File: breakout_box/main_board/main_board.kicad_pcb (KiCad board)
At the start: 2 copper layers, 56 x 120 mm, 45 parts, among them CN1 19PIN_LEMO, Q1 DMP3099L, Q2 MJD122, Q3 MMBT5401, Q4 DMP3099L

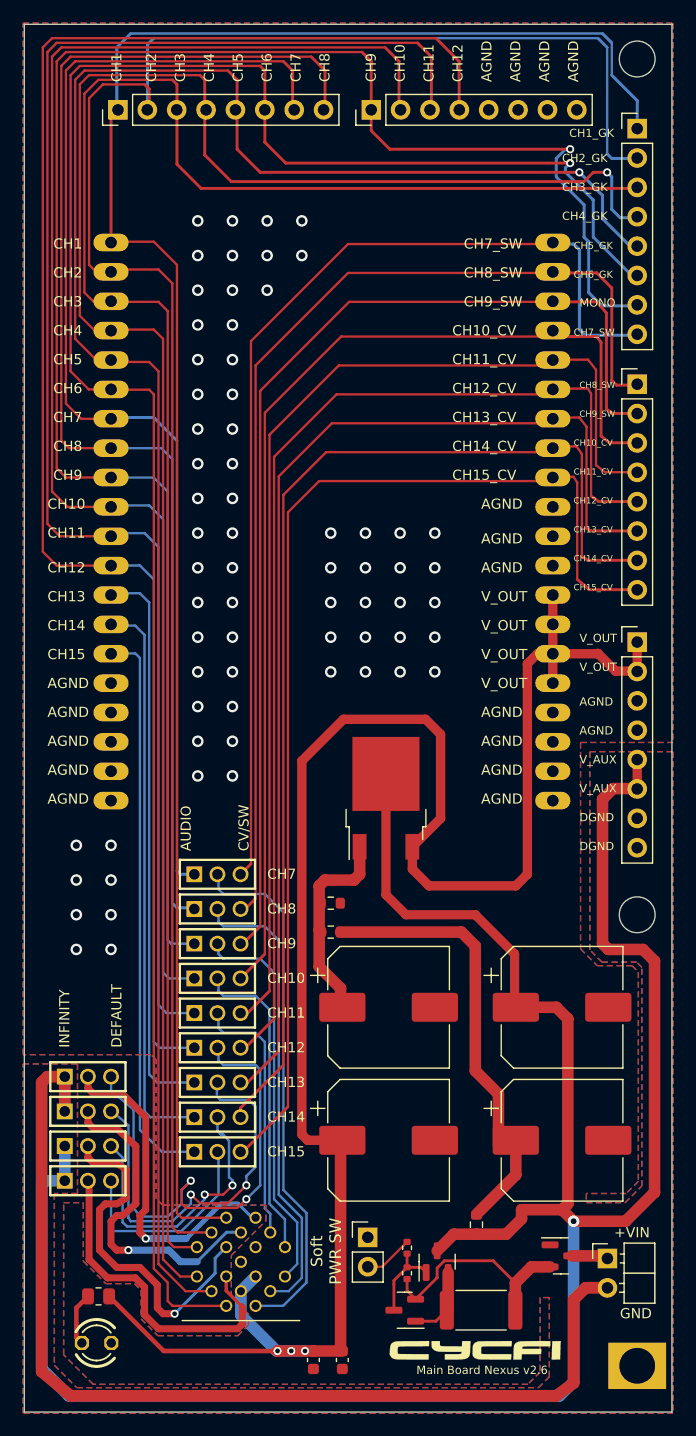
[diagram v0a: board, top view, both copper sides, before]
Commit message: Change the component to C2977785, plus various PCB refinements
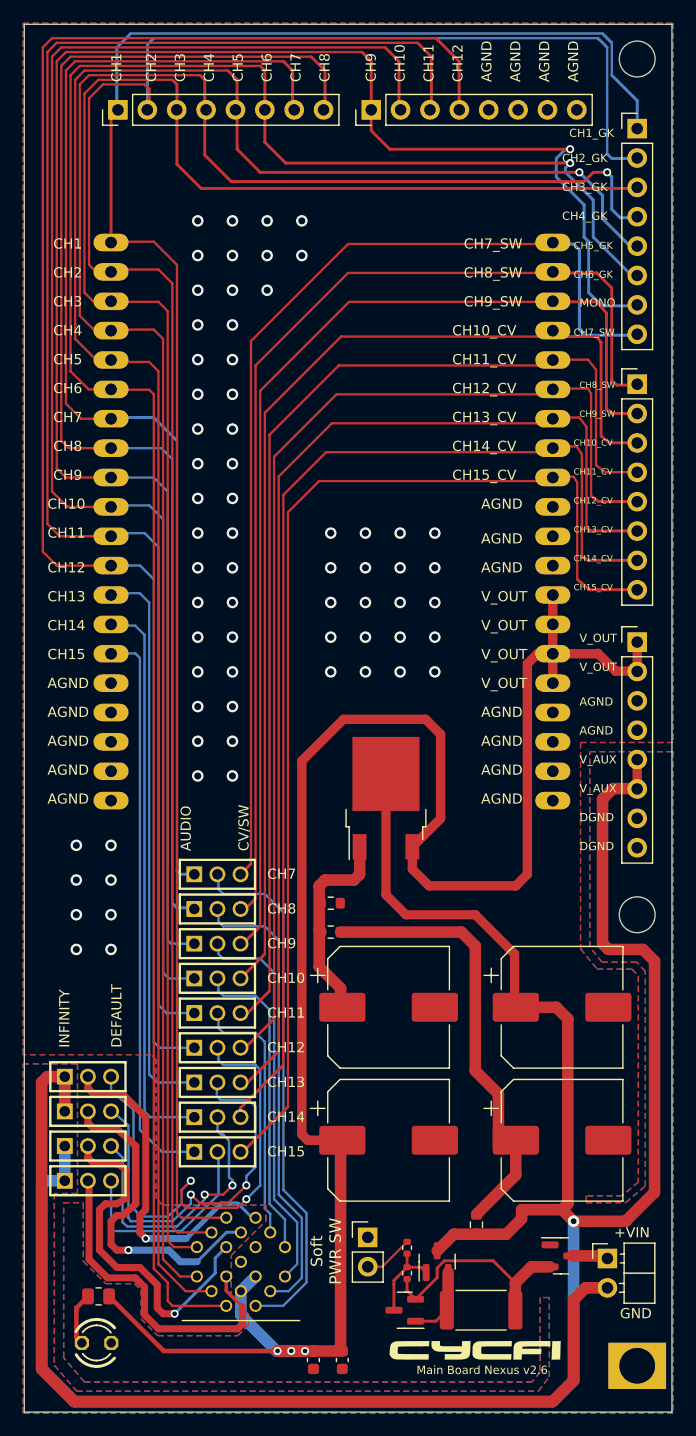
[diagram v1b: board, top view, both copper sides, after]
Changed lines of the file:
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@@
     (effects (font (size 0.536448 0.536448) (thickness 0.073152)) (justify left bottom))
   )
-  (segment (start 168.0011 162.5036) (end 168.0011 155.2989) (width 1.016) (layer "F.Cu") (net 1))
   (segment (start 124.0011 136.0036) (end 124.0011 139.0036) (width 1.016) (layer "F.Cu") (net 1))
+  (segment (start 124.0011 136.0036) (end 122.5011 136.0036) (width 1.016) (layer "F.Cu") (net 1))
+  (segment (start 166.174316 164.1) (end 168.0011 162.273216) (width 1.016) (layer "F.Cu") (net 1))
+  (segment (start 122.0011 136.5036) (end 122.0011 161.3011) (width 1.016) (layer "F.Cu") (net 1))
+  (segment (start 122.5011 136.0036) (end 122.0011 136.5036) (width 1.016) (layer "F.Cu") (net 1))
+  (segment (start 122.0011 161.3011) (end 124.8 164.1) (width 1.016) (layer "F.Cu") (net 1))
   (segment (start 168.0011 155.2989) (end 169.035 154.265) (width 1.016) (layer "F.Cu") (net 1))
-  (segment (start 124.0011 136.0036) (end 122.5011 136.0036) (width 1.016) (layer "F.Cu") (net 1))
+  (segment (start 124.8 164.1) (end 166.174316 164.1) (width 1.016) (layer "F.Cu") (net 1))
   (segment (start 169.035 154.265) (end 170.925 154.265) (width 1.016) (layer "F.Cu") (net 1))
-  (segment (start 166.5011 163.6036) (end 168.0011 162.5036) (width 1.016) (layer "F.Cu") (net 1))
-  (segment (start 124.5011 163.6036) (end 166.5011 163.6036) (width 1.016) (layer "F.Cu") (net 1))
-  (segment (start 122.5011 136.0036) (end 122.0011 136.5036) (width 1.016) (layer "F.Cu") (net 1))
-  (segment (start 122.0011 161.5036) (end 124.5011 163.6036) (width 1.016) (layer "F.Cu") (net 1))
-  (segment (start 122.0011 136.5036) (end 122.0011 161.5036) (width 1.016) (layer "F.Cu") (net 1))
+  (segment (start 168.0011 162.273216) (end 168.0011 155.2989) (width 1.016) (layer "F.Cu") (net 1))
   (via (at 128 119) (size 1) (drill 0.6) (layers "F.Cu" "B.Cu") (free) (net 1))
   (via (at 135.5 95) (size 1) (drill 0.6) (layers "F.Cu" "B.Cu") (free) (net 1))
@@
   (segment (start 170.5011 124.5036) (end 171.0011 125.0036) (width 1) (layer "F.Cu") (net 18))
   (via (at 168.0011 148.5036) (size 1) (drill 0.5) (layers "F.Cu" "B.Cu") (net 18))
-  (segment (start 124.3511 163.6036) (end 166.7964 163.6036) (width 1) (layer "B.Cu") (net 18))
-  (segment (start 122.2511 145.0036) (end 124.0011 145.0036) (width 1) (layer "B.Cu") (net 18))
-  (segment (start 124.3511 163.6036) (end 122.0011 161.2536) (width 1) (layer "B.Cu") (net 18))
-  (segment (start 168.0011 162.3989) (end 168.0011 148.5036) (width 1) (layer "B.Cu") (net 18))
-  (segment (start 166.7964 163.6036) (end 168.0011 162.3989) (width 1) (layer "B.Cu") (net 18))
+  (segment (start 124.0011 145.0036) (end 122.2511 145.0036) (width 1) (layer "B.Cu") (net 18))
+  (segment (start 122.2511 145.0036) (end 122.0011 145.2536) (width 1) (layer "B.Cu") (net 18))
+  (segment (start 122.0011 161.2536) (end 124.8475 164.1) (width 1) (layer "B.Cu") (net 18))
+  (segment (start 122.0011 145.2536) (end 122.0011 161.2536) (width 1) (layer "B.Cu") (net 18))
+  (segment (start 166.2 164.1) (end 168.0011 162.2989) (width 1) (layer "B.Cu") (net 18))
   (segment (start 124.0011 142.0036) (end 124.0011 145.0036) (width 1) (layer "B.Cu") (net 18))
-  (segment (start 122.0011 161.2536) (end 122.0011 145.2536) (width 1) (layer "B.Cu") (net 18))
-  (segment (start 122.0011 145.2536) (end 122.2511 145.0036) (width 1) (layer "B.Cu") (net 18))
+  (segment (start 124.8475 164.1) (end 166.2 164.1) (width 1) (layer "B.Cu") (net 18))
+  (segment (start 168.0011 162.2989) (end 168.0011 148.5036) (width 1) (layer "B.Cu") (net 18))
   (segment (start 140.1011 117.6036) (end 139.2011 118.5036) (width 0.254) (layer "F.Cu") (net 19))
   (segment (start 148.4964 64.0036) (end 166.0711 64.0036) (width 0.2032) (layer "F.Cu") (net 19))
@@
   (segment (start 151.45 152.44) (end 153.6 150.29) (width 0.2) (layer "F.Cu") (net 48))
   (segment (start 150.2 152.44) (end 151.45 152.44) (width 0.2) (layer "F.Cu") (net 48))
-  (zone (net 1) (net_name "GND") (layer "F.Cu") (hatch edge 0.508)
+  (zone (net 1) (net_name "GND") (layers F&B.Cu) (hatch edge 0.508)
     (priority 6)
     (connect_pads (clearance 0.000001))
@@
         (xy 168.6027 107.1052)
         (xy 168.6027 124.961516)
-        (xy 170.043184 126.402)
-        (xy 173.043184 126.402)
-        (xy 173.6027 126.961516)
-        (xy 173.6027 145.045684)
-        (xy 172.543184 146.1052)
-        (xy 169.1027 146.1052)
+        (xy 170.043184 126.702)
+        (xy 173.043184 126.702)
+        (xy 173.6027 127.3)
+        (xy 173.6027 145.1)
+        (xy 172.2 146.3052)
+        (xy 169.1027 146.3052)
         (xy 169.1027 146.902)
-        (xy 172.459016 146.902)
-        (xy 173.8995 145.461516)
-        (xy 173.8995 126.545684)
+        (xy 172.5 146.9)
+        (xy 174.1995 145.461516)
+        (xy 174.2 126.9)
         (xy 173.459016 126.1052)
         (xy 170.459016 126.1052)
-        (xy 169.3995 125.045684)
+        (xy 169.4 124.8)
         (xy 169.3995 107.902)
         (xy 176.6027 107.902)
@@
         (xy 123.1027 146.1052)
         (xy 123.1027 160.961516)
-        (xy 125.043184 162.902)
-        (xy 164.959016 162.902)
+        (xy 125.043184 163.202)
+        (xy 164.959016 163.202)
         (xy 165.8995 161.961516)
         (xy 165.8995 155.1052)
         (xy 165.1027 155.1052)
         (xy 165.1027 161.545684)
-        (xy 164.043184 162.6052)
-        (xy 126.459016 162.6052)
-        (xy 123.8995 160.045684)
+        (xy 164.4 162.4052)
+        (xy 125.7 162.4052)
+        (xy 123.9 160.3)
         (xy 123.8995 146.902)
         (xy 125.6027 146.902)
-        (xy 125.6027 151.961516)
-        (xy 127.543184 153.902)
-        (xy 130.043184 153.902)
-        (xy 130.6027 154.461516)
-        (xy 130.6027 156.961516)
-        (xy 132.043184 158.402)
-        (xy 138.959016 158.402)
-        (xy 139.8995 157.461516)
-        (xy 139.8995 156.545684)
-        (xy 138.3995 155.045684)
-        (xy 138.3995 151.461516)
-        (xy 141.3995 148.461516)
-        (xy 141.3995 147.1052)
-        (xy 132.459016 147.1052)
-        (xy 131.8995 146.545684)
-        (xy 131.8995 134.545684)
-        (xy 131.459016 134.1052)
-        (xy 120.3995 134.1052)
-        (xy 120.3995 44.902)
-        (xy 176.6027 44.902)
-      )
-    )
-  )
-  (zone (net 1) (net_name "GND") (layer "B.Cu") (hatch edge 0.508)
-    (priority 6)
-    (connect_pads (clearance 0.000001))
-    (min_thickness 0.1016) (filled_areas_thickness no)
-    (fill yes (thermal_gap 0.2532) (thermal_bridge_width 0.2532))
-    (polygon
-      (pts
-        (xy 176.6027 107.1052)
-        (xy 168.6027 107.1052)
-        (xy 168.6027 124.961516)
-        (xy 170.043184 126.402)
-        (xy 173.043184 126.402)
-        (xy 173.6027 126.961516)
-        (xy 173.6027 145.045684)
-        (xy 172.543184 146.1052)
-        (xy 169.1027 146.1052)
-        (xy 169.1027 146.902)
-        (xy 172.459016 146.902)
-        (xy 173.8995 145.461516)
-        (xy 173.8995 126.545684)
-        (xy 173.459016 126.1052)
-        (xy 170.459016 126.1052)
-        (xy 169.3995 125.045684)
-        (xy 169.3995 107.902)
-        (xy 176.6027 107.902)
-        (xy 176.6027 165.1052)
-        (xy 120.3995 165.1052)
-        (xy 120.3995 134.902)
-        (xy 125.1027 134.902)
-        (xy 125.1027 146.1052)
-        (xy 123.1027 146.1052)
-        (xy 123.1027 160.961516)
-        (xy 125.043184 162.902)
-        (xy 164.959016 162.902)
-        (xy 165.8995 161.961516)
-        (xy 165.8995 155.1052)
-        (xy 165.1027 155.1052)
-        (xy 165.1027 161.545684)
-        (xy 164.043184 162.6052)
-        (xy 126.459016 162.6052)
-        (xy 123.8995 160.045684)
-        (xy 123.8995 146.902)
-        (xy 125.6027 146.902)

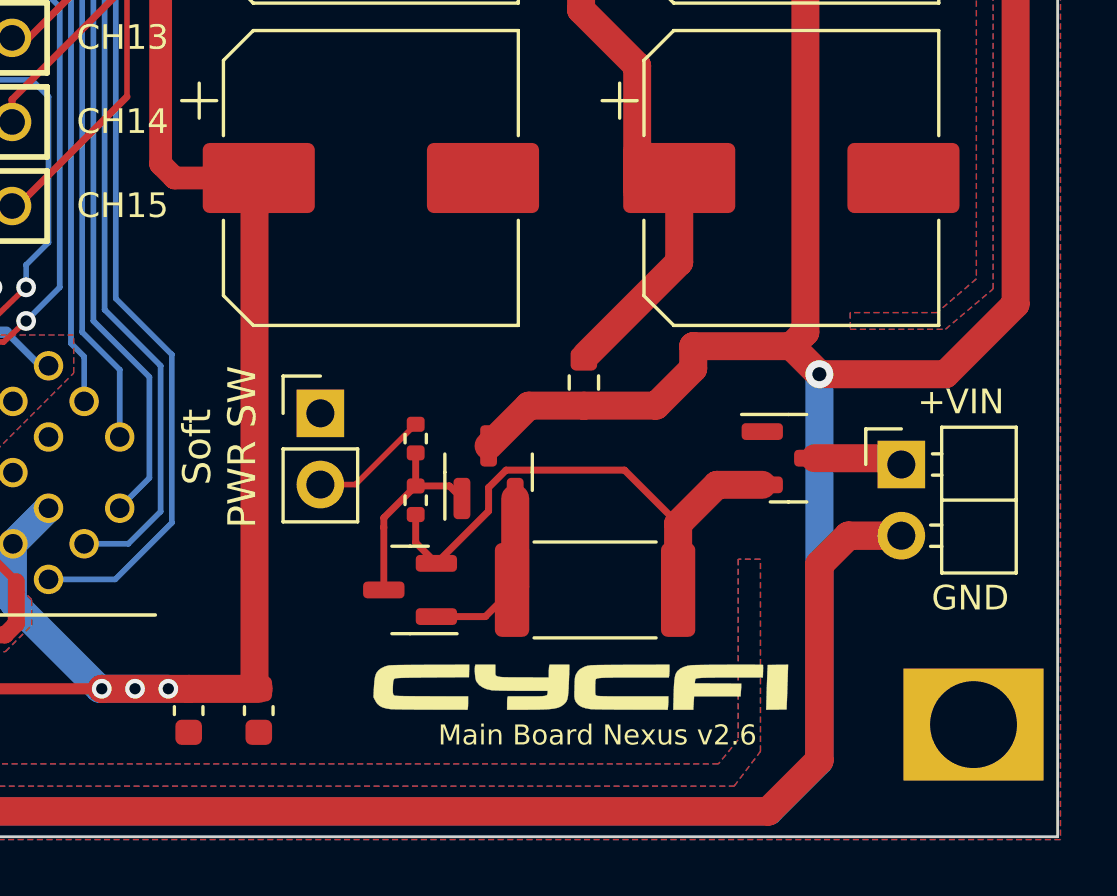
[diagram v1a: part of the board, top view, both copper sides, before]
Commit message: Use AOZ1360AIL load switch
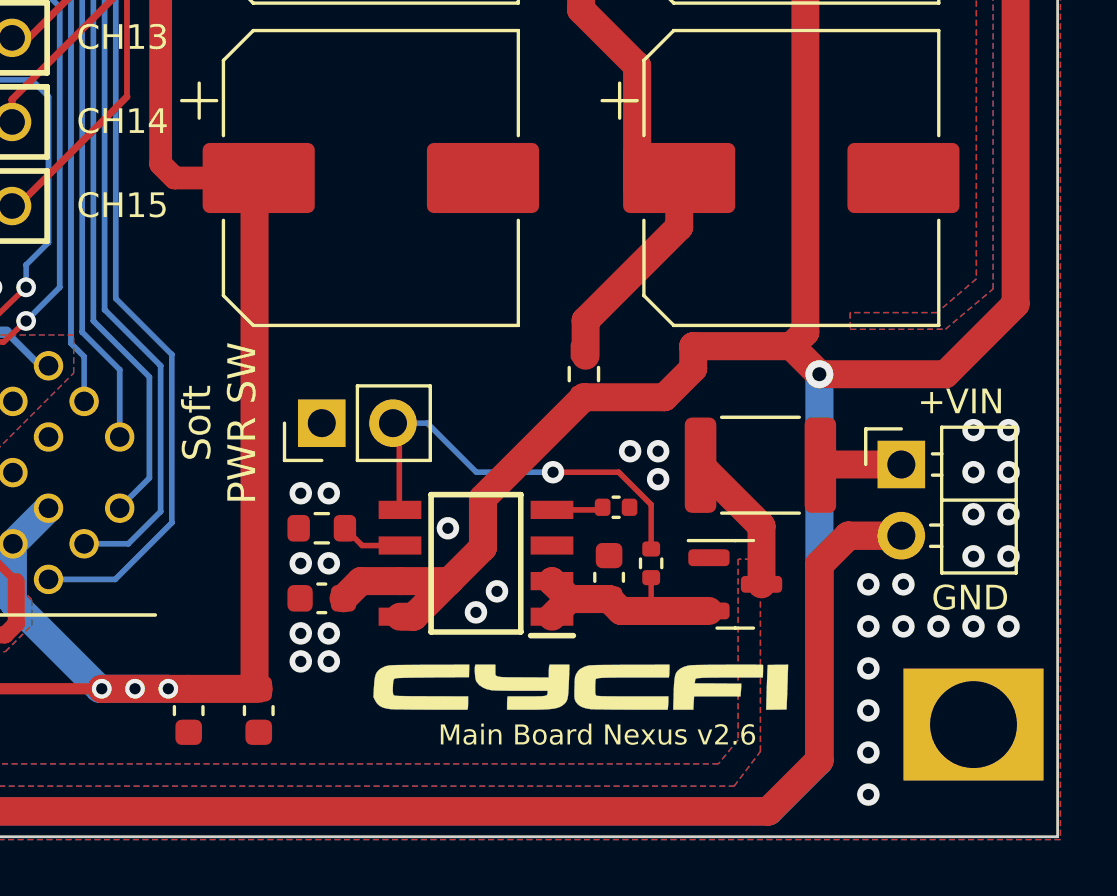
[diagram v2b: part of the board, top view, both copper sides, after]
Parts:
- removed Q4: DMP3099L, Package_TO_SOT_SMD:SOT-23
- removed R7: 0.36R 2 Watts, Resistor_SMD:R_2512_6332Metric
- added C7: 1uF, Capacitor_SMD:C_0603_1608Metric, F.Cu at (160.5, 155.8)
- added C8: 1nF, Capacitor_SMD:C_0402_1005Metric, F.Cu at (160.8, 153.2)
- added C9: 1uF, Capacitor_SMD:C_0603_1608Metric, F.Cu at (150.2, 156.5)
- added F1: 2A, Fuse:Fuse_1812_4532Metric, F.Cu at (165.9, 151.8)
- Q3: value MMBT5401 -> AOZ1360AIL; footprint Package_TO_SOT_SMD:SOT-23 -> cycfi_library:SOIC127P600X175-8N
- R5: value 100K -> 91k; footprint Resistor_SMD:R_0402_1005Metric -> Resistor_SMD:R_0603_1608Metric
- moved R6 9.51 mm to (162.0, 155.2)
- moved Q1 4.88 mm to (165.0, 156.0)
- moved R5 3.50 mm to (150.2, 154.0), turned to 0 degrees
- moved Q3 2.53 mm to (155.8, 155.2)
- moved H5 0.35 mm to (150.2, 150.2), turned to 90 degrees
- moved R1 0.30 mm to (159.6, 148.5)
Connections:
- H6 pad 1: Net-(Q1-Pad3) -> Net-(H6-Pad1)
- Q1 pad 2: Net-(Q1-Pad2) -> /RPP
- Q3 pad 1: Net-(Q3-Pad1) -> /RPP
- Q3 pad 2: Net-(Q1-Pad2) -> /RPP
- Q3 pad 3: Net-(Q3-Pad3) -> GND
- R5 pad 1: Net-(Q1-Pad2) -> GND
- R5 pad 2: Net-(Q3-Pad3) -> Net-(Q3-Pad6)
- R6 pad 1: Net-(Q3-Pad3) -> /RPP
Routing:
- net Net-(Q1-Pad2): track 19.3 -> 0.00 mm
- net Net-(H5-Pad2): track 4.29 -> 15.2 mm, vias 0 -> 1
- net V_AUX: track 198.7 -> 209.5 mm
- net /RPP: track 0.00 -> 8.15 mm
- net Net-(Q3-Pad3): track 7.20 -> 0.00 mm
- net Net-(Q3-Pad1): track 6.40 -> 0.00 mm
- net Net-(H6-Pad1): track 0.00 -> 2.90 mm
- net Net-(Q3-Pad6): track 0.00 -> 2.22 mm
- net Net-(Q1-Pad3): track 3.18 -> 5.15 mm
- net Net-(C8-Pad1): track 0.00 -> 1.85 mm
- net GND: vias 67 -> 100

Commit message: Updates for PCBA and panelization
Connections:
- GND_HOLE pad : GND -> (no net)
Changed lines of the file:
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@@
       (effects (font (size 1.27 1.27) (thickness 0.15)))
     )
-    (pad "" thru_hole rect locked (at 0 0) (size 5 4) (drill 3.1) (layers *.Cu "B.Mask")
-      (net 1 "GND"))
+    (fp_circle (center 0 0) (end 1.627882 0) (layer "F.Mask") (width 0.12) (fill solid))
+    (pad "" thru_hole rect locked (at 0 0) (size 5 4) (drill 3.1) (layers *.Cu "B.Mask"))
   )
   (footprint "Connector_PinHeader_2.54mm:PinHeader_1x08_P2.54mm_Vertical" (layer "F.Cu")

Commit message: Production run May 2025
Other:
- board text removed: "JLCJLCJLCJLC"
